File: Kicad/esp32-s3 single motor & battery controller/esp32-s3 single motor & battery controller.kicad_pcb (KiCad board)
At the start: 4 copper layers, 44.9 x 42 mm, 135 parts, among them J1 JST SH SM04B, J2 7 pin FPC 0.3mm, J3 Conn_01x03, J4 Conn_01x03, J5 Batt Balance connector, Q1 NMOS,12v, Q2 NMOS, 12v, Q3 NMOS,12v,PPak, Q4 NMOS, 12v, Q5 NMOS, 12v, Q7 NMOS,12v,PPak, SW1 KMR2, SW2 KMR2, U2 AP63203WU, U3 BQ76905RGRR, U4 BQ24780SRUYR, U5 ESP32-S3, U6 74HC595, Y1 40mhz, 10ppm

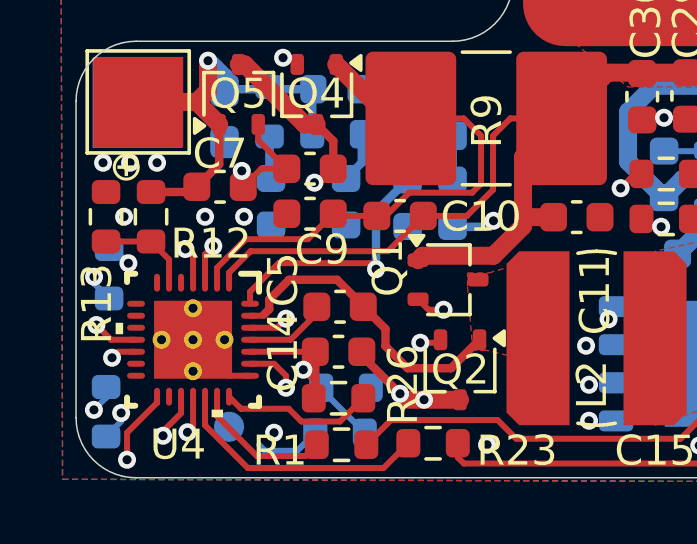
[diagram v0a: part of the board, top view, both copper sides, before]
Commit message: Routed pullup resistors, replace Bat Pres trace with pad
I now have several lines routed on the ground plane, but I tried to minimize the used space
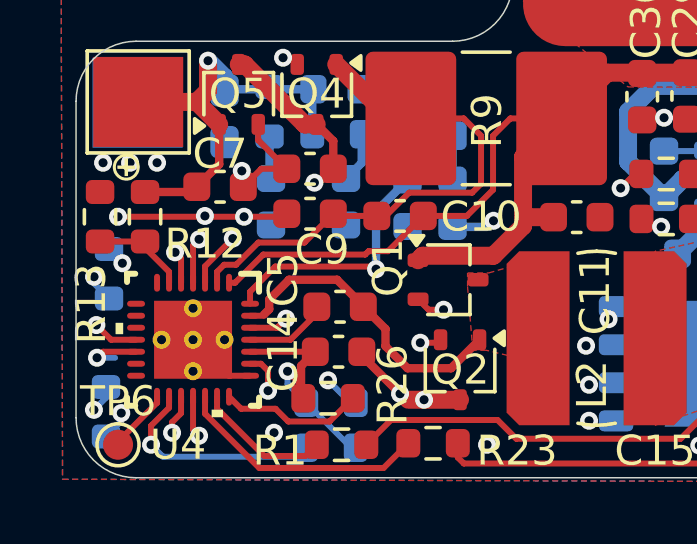
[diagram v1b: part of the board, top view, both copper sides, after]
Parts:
- TP6: moved to F.Cu
- moved TP6 3.75 mm to (109.5, 130.9), turned to 0 degrees
- moved R8 0.71 mm to (116.6, 129.5)
- moved R18 0.58 mm to (116.6, 131.0)
- moved R26 0.35 mm to (116.5, 129.3)
- moved R12 0.20 mm to (110.4, 123.3)
- moved R13 0.20 mm to (108.9, 123.3)
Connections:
- TP6 pad 1: /PSU/Low -> Net-(U4-BATPRES_N)
- U4 pad 15: /PSU/Low -> Net-(U4-BATPRES_N)
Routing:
- net /PSU/Low: track 50.3 -> 18.5 mm, vias 3 -> 2
- net Net-(U4-ACOK): track 0.00 -> 14.6 mm, vias 0 -> 2
- net GNDPWR: track 23.3 -> 29.0 mm
- net Net-(U4-TB_STAT_N): track 2.21 -> 7.68 mm, vias 0 -> 1
- net Net-(U4-BATPRES_N): track 0.00 -> 2.14 mm
- net Net-(U4-ACDRV): track 5.71 -> 7.75 mm
- net /SCL1: track 81.5 -> 83.5 mm
- net Net-(U4-CMSRC): track 9.62 -> 11.0 mm
- net /PSU/REGN: track 7.79 -> 8.65 mm
- net Net-(Q4-G): track 14.4 -> 15.0 mm
- net Net-(Q2-G): track 7.58 -> 8.20 mm

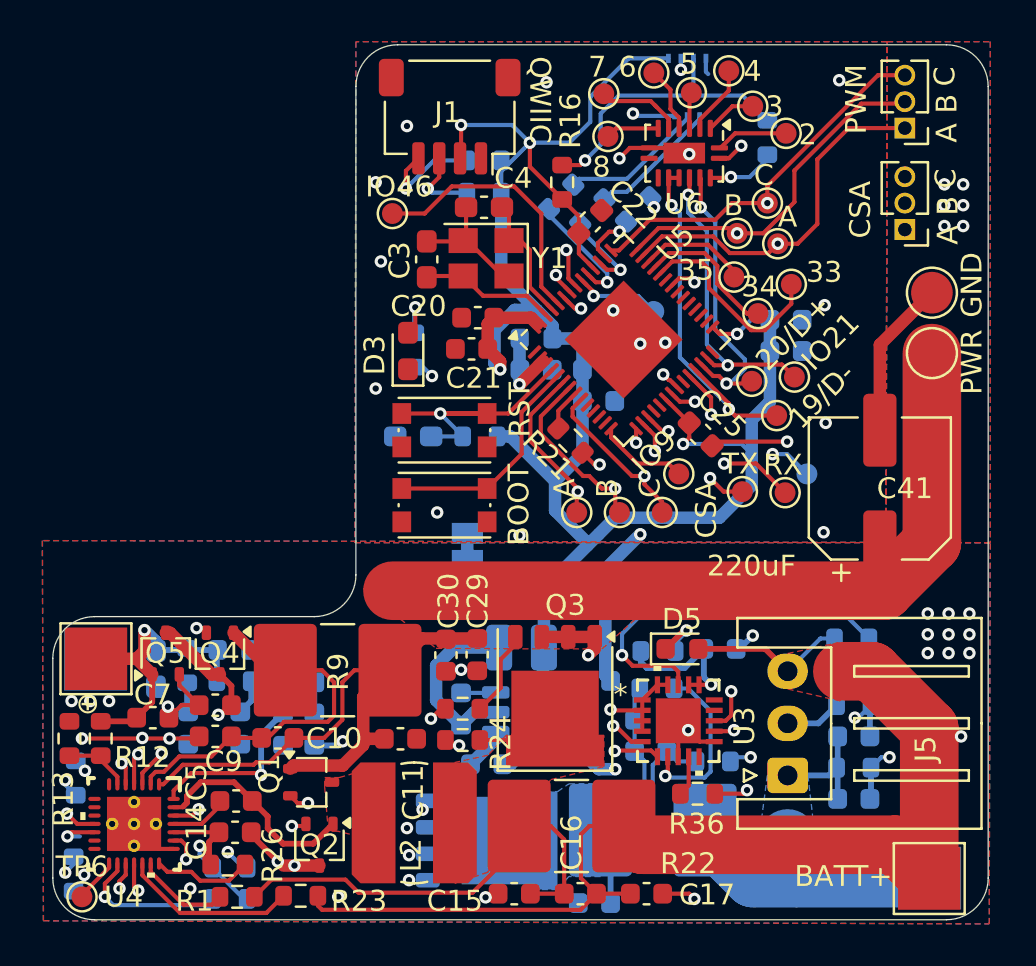
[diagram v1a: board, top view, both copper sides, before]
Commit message: Silkscreen and smd clearance cleanup
Everything was complete, but I identified a new issue on the board to fix soon. I will have to switch the battery balance chip to the other side of the board to be closer to the current sense resistor and minimize losses.
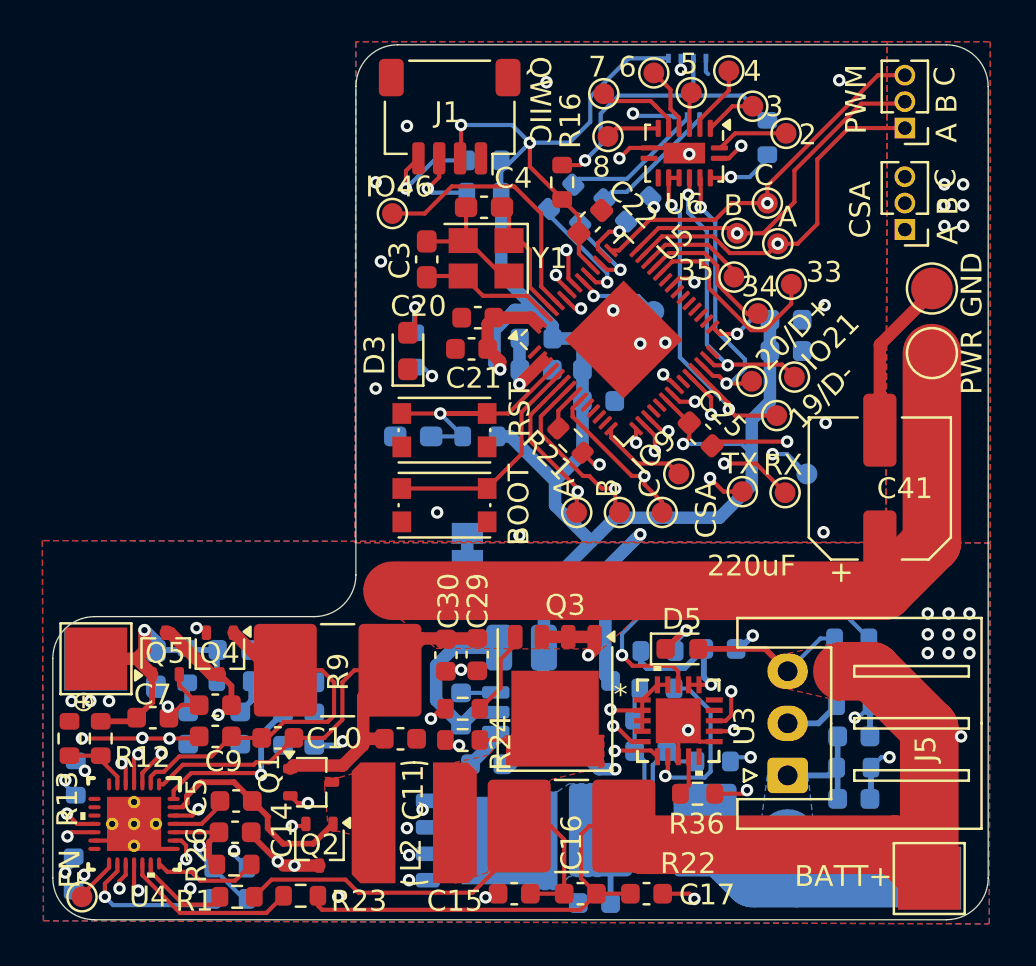
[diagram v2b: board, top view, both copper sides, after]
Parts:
- moved R26 0.30 mm to (116.8, 129.3)
- moved H5 0.20 mm to (150.3, 101.7)
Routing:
- net GNDPWR: track 29.0 -> 31.4 mm
- net /SCL1: track 83.5 -> 82.9 mm
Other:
- board text added: "EN"

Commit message: Swapped sides for battery balance IC
This actually simplifies routing a lot, since the current sense lines are on the same side.
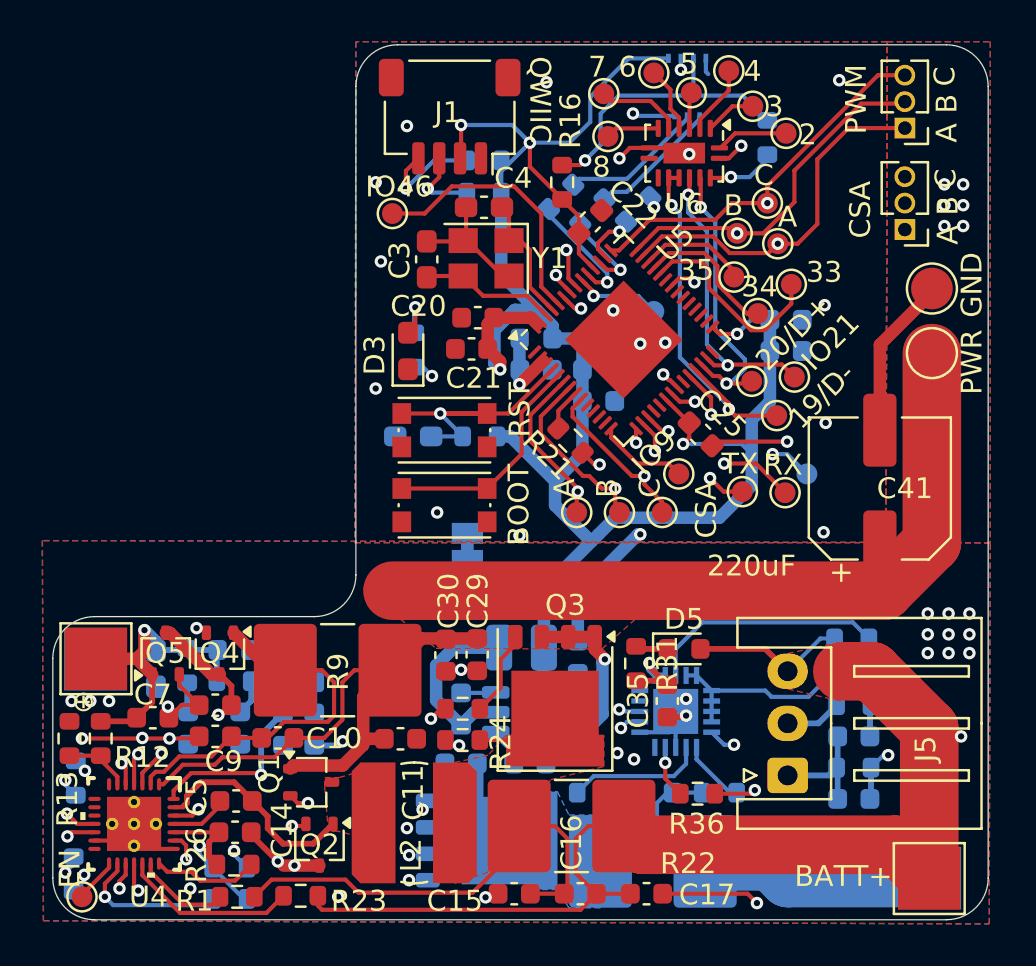
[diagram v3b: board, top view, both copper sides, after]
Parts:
- removed C32: 100pF, Capacitor_SMD:C_0603_1608Metric
- C35, R31: moved to F.Cu
- U3: moved to B.Cu
- moved C38 9.27 mm to (127.7, 124.5)
- moved R30 5.83 mm to (134.1, 125.9), turned to 0 degrees
- moved C35 3.55 mm to (137.6, 121.5), turned to -90 degrees
- moved C33 3.51 mm to (137.1, 125.9)
- moved C28 2.08 mm to (131.0, 124.5)
- moved R29 1.53 mm to (140.1, 125.9)
- moved R27 1.50 mm to (136.9, 129.2)
- moved C27 1.39 mm to (133.3, 119.4), turned to 90 degrees
- moved R31 1.21 mm to (136.1, 119.7), turned to -90 degrees
- moved U3 0.47 mm to (138.0, 122.0), turned to 180 degrees
- moved R32 0.44 mm to (133.3, 122.5)
- moved D5 0.10 mm to (138.4, 119.0)
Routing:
- net /PSU/mid: track 22.1 -> 13.5 mm, vias 2 -> 0
- net /SDA1: track 78.1 -> 70.3 mm
- net /PSU/Low: track 18.5 -> 11.5 mm
- net /SCL1: track 82.9 -> 76.0 mm
- net Net-(U3-SRP): track 9.89 -> 3.16 mm, vias 2 -> 0
- net /PSU/Up: track 18.8 -> 12.9 mm, vias 1 -> 0
- net /MOTORPWR: track 81.3 -> 75.9 mm, vias 2 -> 1
- net /PSU/BATT-: track 23.3 -> 18.3 mm
- net GNDPWR: track 31.4 -> 34.7 mm, vias 31 -> 33
- net Net-(U3-BAT): track 6.99 -> 4.20 mm
- net /PSU/BATT+: track 90.9 -> 93.1 mm
- net Net-(U3-SRN): track 8.41 -> 6.59 mm, vias 1 -> 0
- net GND: track 24.7 -> 22.9 mm
- net Net-(D5-K): track 2.93 -> 1.56 mm, vias 1 -> 0
- net Net-(Q7-S): track 12.9 -> 11.9 mm
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- removed copper zone on B.Cu, net /PSU/BATT-

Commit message: Fixing routing issues after change
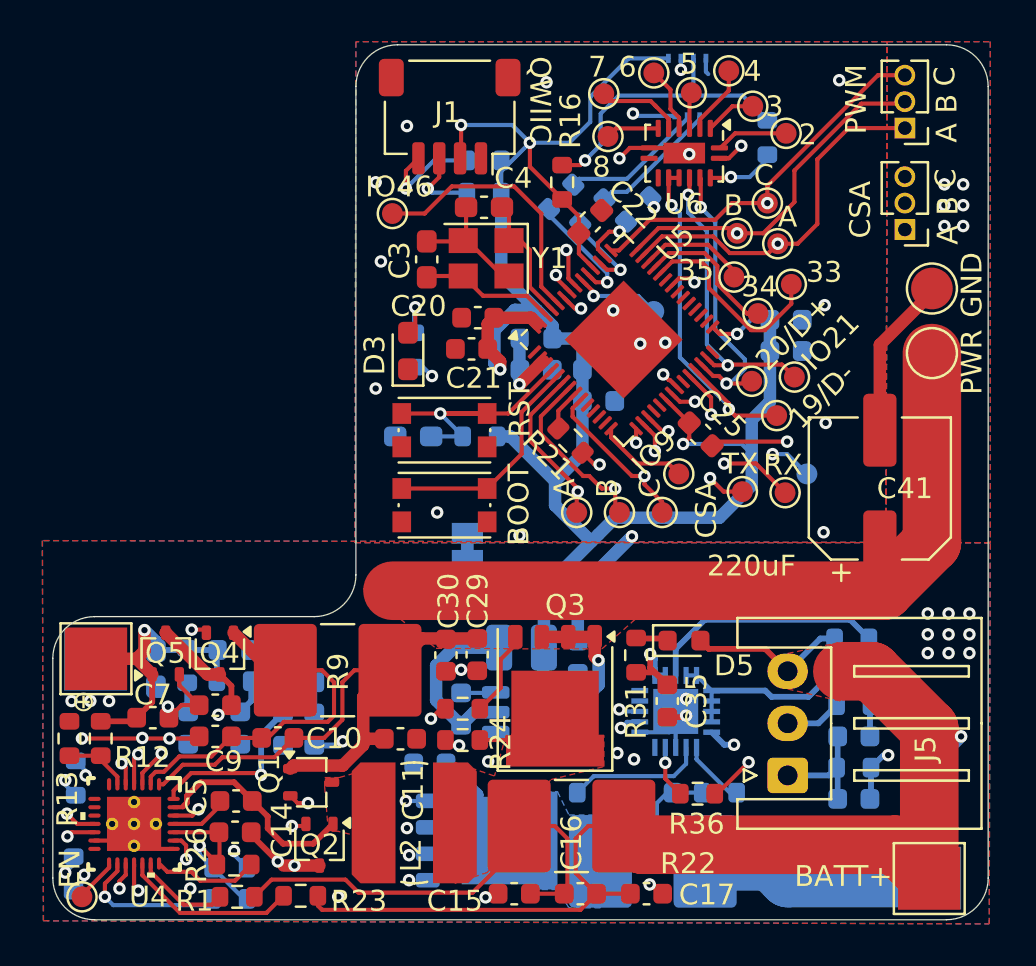
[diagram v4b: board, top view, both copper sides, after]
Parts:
- removed R32: 10k, Resistor_SMD:R_0603_1608Metric
- moved C28 3.05 mm to (133.3, 122.5), turned to -90 degrees
- moved C38 1.50 mm to (126.2, 124.5)
- moved D5 0.40 mm to (138.4, 118.6)
- moved R31 0.40 mm to (136.1, 119.3)
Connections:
- U2 pad 2: Net-(U2-EN) -> /MOTORPWR
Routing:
- net GNDPWR: track 34.7 -> 29.0 mm, vias 33 -> 34
- net /MOTORPWR: track 75.9 -> 73.8 mm
- net Net-(U2-EN): track 1.81 -> 0.00 mm
- net /SDA1: track 70.3 -> 72.1 mm
- net Net-(Q7-G): track 18.9 -> 20.5 mm
- net /SCL1: track 76.0 -> 77.1 mm
- net Net-(U3-BAT): track 4.20 -> 5.18 mm
- net Net-(Q7-S): track 11.9 -> 12.5 mm
- net /PSU/BATT+: track 93.1 -> 92.5 mm

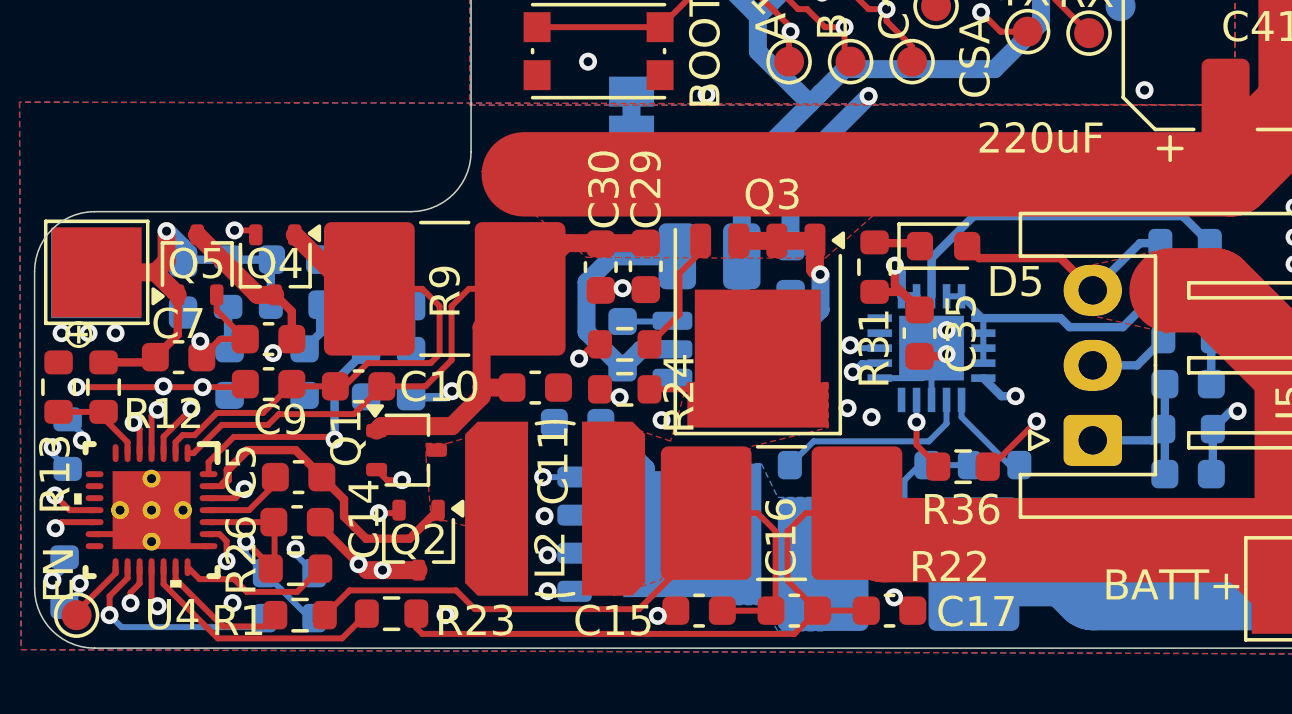
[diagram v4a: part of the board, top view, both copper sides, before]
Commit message: Finished design
I speced out the proper diodes, routed the wires away from the inductor, added more ground vias, and did some general cleanup.
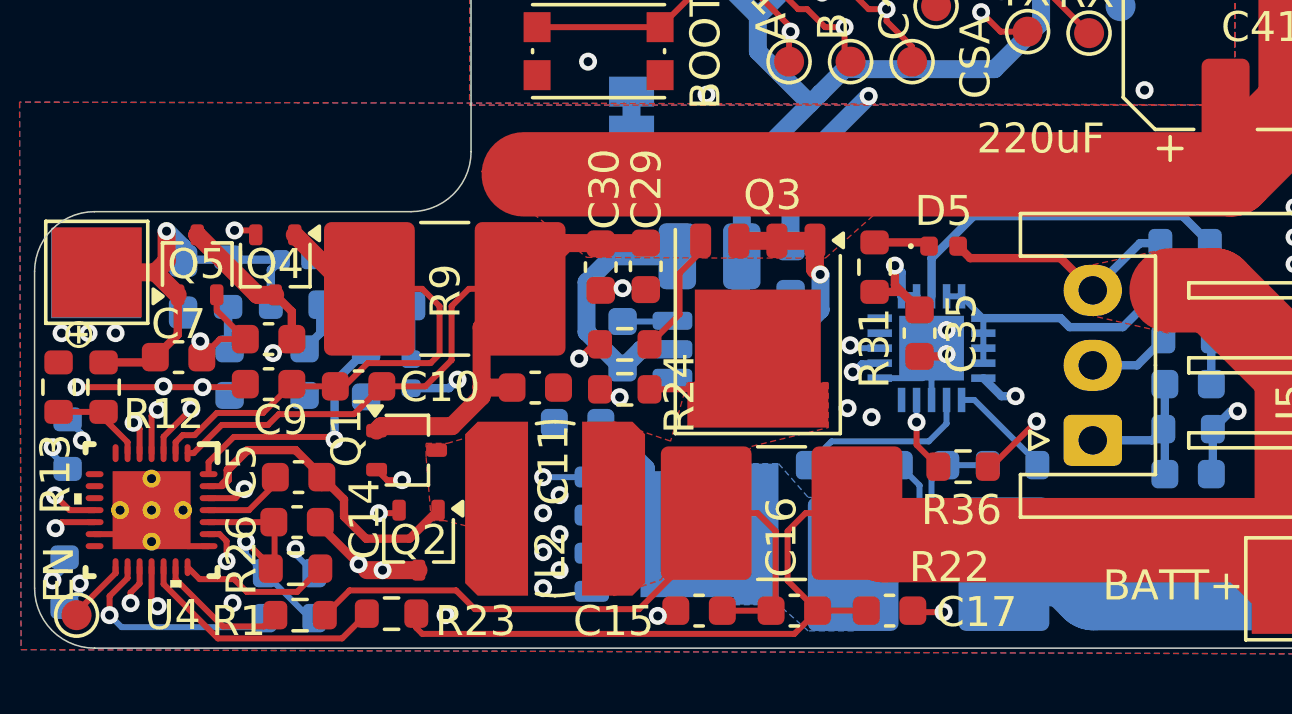
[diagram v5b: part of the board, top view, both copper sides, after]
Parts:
- D2, D4, D5: value D -> GSDH3005; footprint Diode_SMD:D_0603_1608Metric -> Diode_SMD:D_0402_1005Metric
- J1: value JST SH SM04B -> JST SH SM04B/Qwiic
- J5: value Batt Balance connector -> JST XH-S
- L2: value 5.6uH, 2.2A < sat -> 5.6uH Bourns SDE0604A
- L3: value 4.7uH -> 4.7uH, MAMK2520T4R7M
- Q1: value NMOS,12v -> PJA3430
- Q2, Q4, Q5: value NMOS, 12v -> PJA3430
- Q3, Q7: value NMOS,12v,PPak -> Vishay sir404dp
- R22: value 5mOhm, CS -> 5mOhm, CS wshp2818
- R27: value 1mOhm, CS -> 1mOhm, CS wshp2818
- R9: value 5mOhm CS -> 5mOhm CS wshp2818
- moved R27 1.00 mm to (137.9, 129.2)
- moved C33 0.60 mm to (137.7, 125.9)
- moved R29 0.60 mm to (140.7, 125.9)
- moved R30 0.60 mm to (134.7, 125.9)
- moved Q7 0.58 mm to (129.4, 128.2)
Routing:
- net /SCL1: track 77.1 -> 78.5 mm
- net Net-(U4-BATSRC): track 22.0 -> 23.2 mm
- net /PSU/BATT-: track 18.3 -> 17.1 mm
- net Net-(D2-K): track 5.27 -> 5.88 mm
- net Net-(U3-SRN): track 6.59 -> 5.99 mm
- net Net-(Q7-G): track 20.5 -> 21.1 mm
- net GNDPWR: track 29.0 -> 29.2 mm, vias 34 -> 36
